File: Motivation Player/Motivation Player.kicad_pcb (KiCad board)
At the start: 2 copper layers, 18 parts, among them U1 LM386

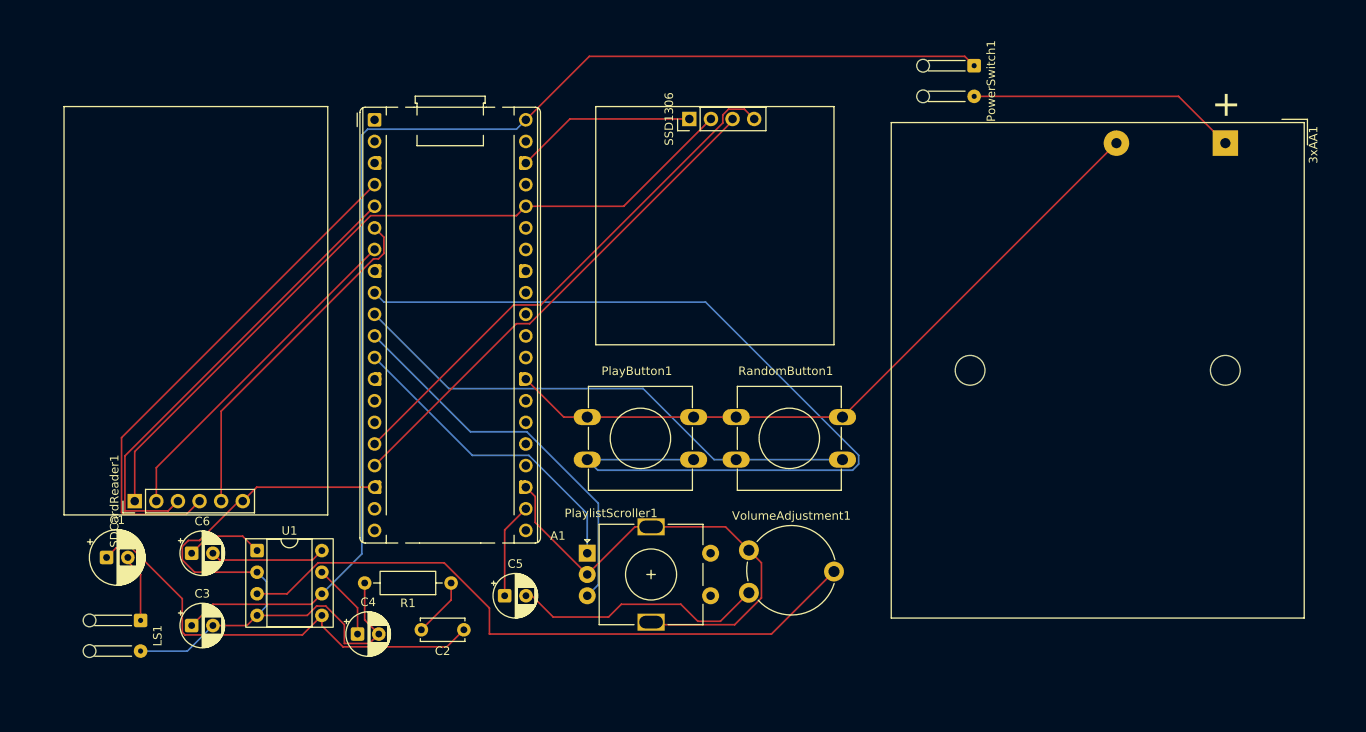
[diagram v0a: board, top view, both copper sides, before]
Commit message: Finished PCB (actually)
Fixed up parts of the PCB using DRC
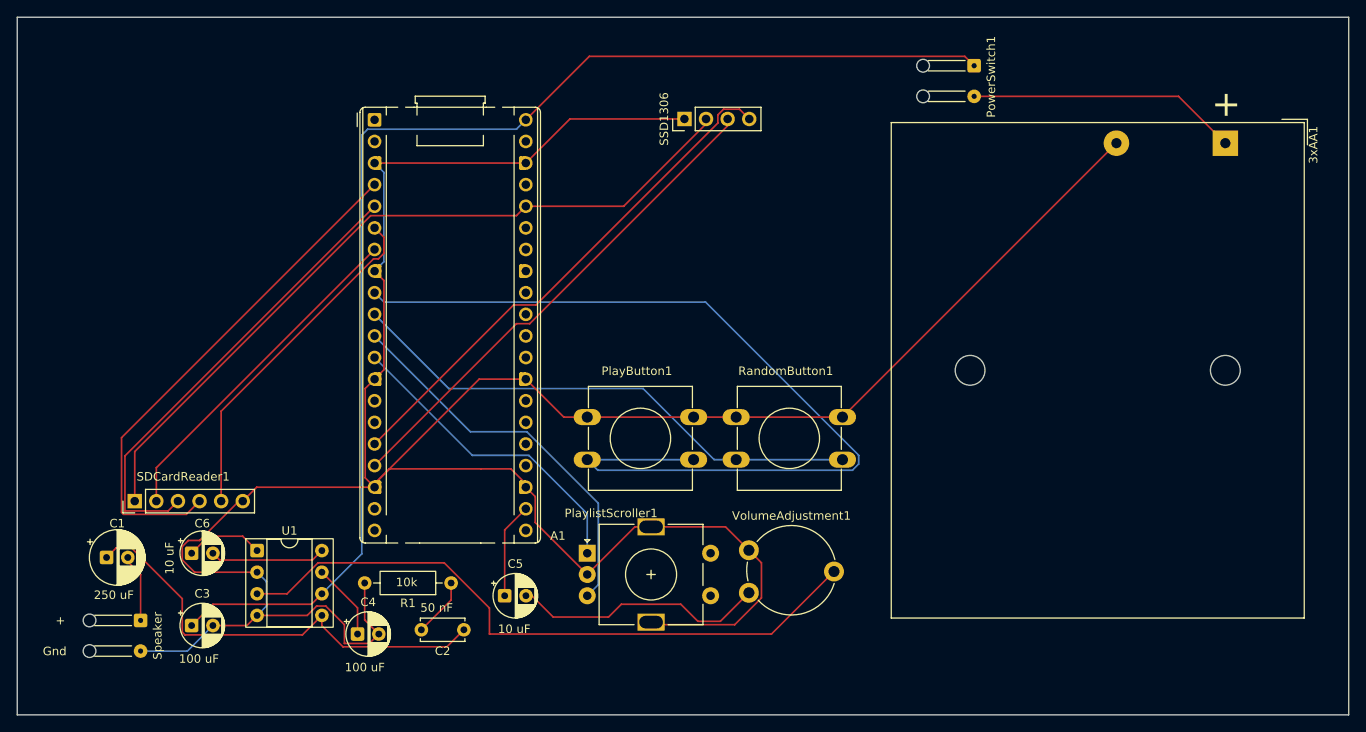
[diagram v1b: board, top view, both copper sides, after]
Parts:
- moved SSD1306 0.58 mm to (152.4, 70.5)
- renumbered LS1 to Speaker
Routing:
- net GNDREF: track 245.2 -> 346.1 mm
- net Net-(A1-GPIO12): track 62.0 -> 61.4 mm
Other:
- board outline added: 156.5 x 82 mm
- board text added: "+"
- board text added: "10 uF"
- board text added: "100 uF"
- board text added: "10k"
- board text added: "250 uF"
- board text added: "50 nF"
- board text added: "Gnd"

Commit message: CAD models
Finished making the CAD models for the enclosure of the Motivation Player (also added an assembled version of it -- some parts aren't correct due to not having all the right parts needed
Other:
- board text added: "Motivation Player Made by Gavin Wu"
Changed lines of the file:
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@@
+		)
+	)
+	(gr_text "Motivation Player\nMade by Gavin Wu"
+		(at 79 64.5 0)
+		(layer "F.SilkS")
+		(effects
+			(font
+				(size 1 1)
+				(thickness 0.1)
+			)
+			(justify left bottom)
 		)
 	)
